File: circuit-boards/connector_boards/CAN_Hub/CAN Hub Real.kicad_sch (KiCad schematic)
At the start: 10 parts, among them J1 Conn_01x02_Pin, J2 Conn_01x02_Pin, J3 Conn_01x02_Pin, J4 Conn_01x02_Pin, J5 Conn_01x02_Pin, J6 Conn_01x02_Pin

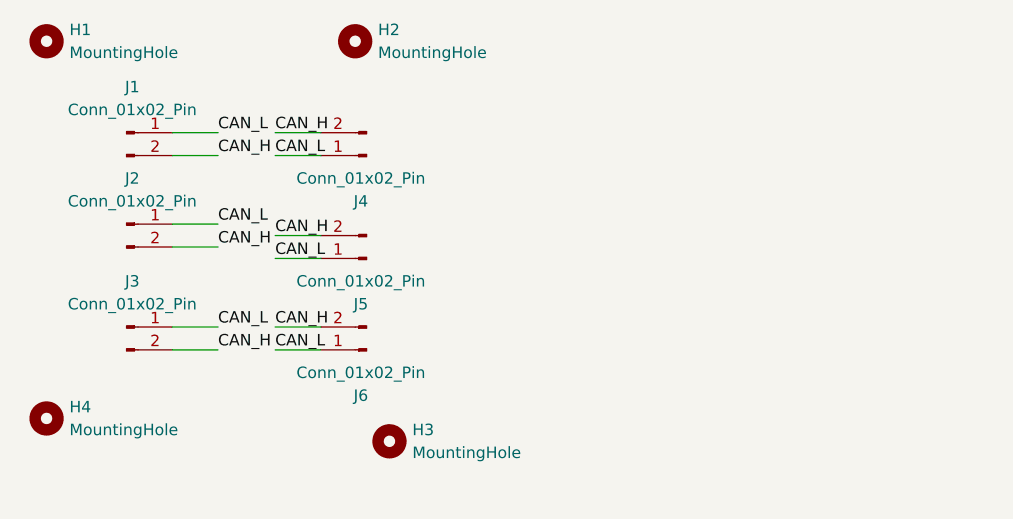
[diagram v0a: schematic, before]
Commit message: more compact layout, and better routing
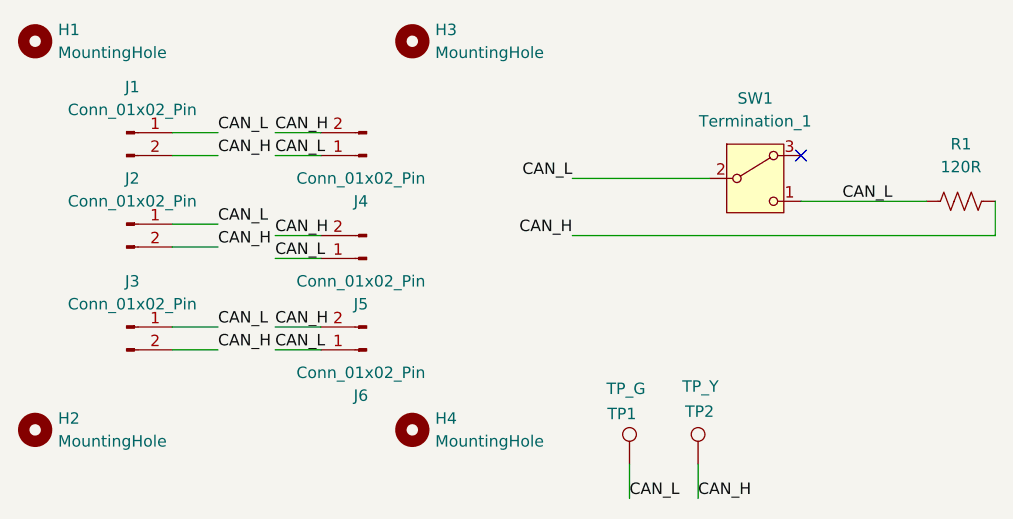
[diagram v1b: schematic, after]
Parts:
- added R1: 120R, Resistor_SMD:R_0805_2012Metric, symbol Device:R_US
- added SW1: Termination_1, Button_Switch_SMD:Nidec_Copal_CAS-120A, symbol Switch:SW_Nidec_CAS-120A1
- added TP1: TP_G, TestPoint:TestPoint_Pad_2.0x2.0mm, symbol Connector:TestPoint
- added TP2: TP_Y, TestPoint:TestPoint_Pad_2.0x2.0mm, symbol Connector:TestPoint
- H1: footprint MountingHole:MountingHole_2.1mm -> MountingHole:MountingHole_3.175
- H2: renamed from H4; footprint MountingHole:MountingHole_2.1mm -> MountingHole:MountingHole_3.175
- H3: renamed from H2; footprint MountingHole:MountingHole_2.1mm -> MountingHole:MountingHole_3.175
- H4: renamed from H3; footprint MountingHole:MountingHole_2.1mm -> MountingHole:MountingHole_3.175
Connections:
- net CAN_H: now also R1.2, TP2.1
- net CAN_L: now also R1.1, SW1.1 (C), SW1.2 (B), TP1.1
- no-connect marks 0 -> 1
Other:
- moved on the sheet: H1, H2, H3, H4
